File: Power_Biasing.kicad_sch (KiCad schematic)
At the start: 1 part

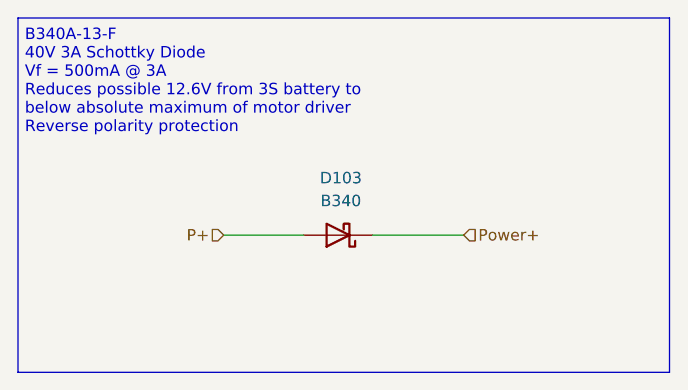
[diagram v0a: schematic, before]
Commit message: added fuse and made power nets thicker
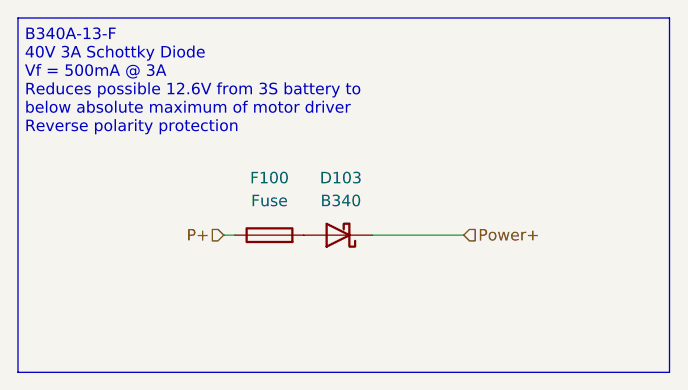
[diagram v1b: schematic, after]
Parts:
- added F100: Fuse, Fuse:Fuse_1206_3216Metric, symbol Device:Fuse
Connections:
- net P+: now also F100.1; no longer D103.2 (A)
- new net: D103.2 (A), F100.2
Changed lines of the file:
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@@
 	(wire
 		(pts
-			(xy 139.7 96.52) (xy 148.59 96.52)
+			(xy 139.7 96.52) (xy 140.97 96.52)
 		)
 		(stroke
@@
 					(unit 1)
 				)
+			)
+		)
+	)
+	(symbol
+		(lib_id "Device:Fuse")
+		(at 144.78 96.52 90)
+		(unit 1)
+		(exclude_from_sim no)
+		(in_bom yes)
+		(on_board yes)
+		(dnp no)
+		(fields_autoplaced yes)
+		(property "Reference" "F100"
+			(at 144.78 90.17 90)
+			(effects
+				(font
+					(size 1.27 1.27)
+				)
+			)
+		)
+		(property "Value" "Fuse"
+			(at 144.78 92.71 90)
+			(effects
+				(font
+					(size 1.27 1.27)
+				)
+			)
+		)
+		(property "Footprint" "Fuse:Fuse_1206_3216Metric"
+			(at 144.78 98.298 90)
+			(effects
+				(font
+					(size 1.27 1.27)
+				)
+				(hide yes)
+			)
+		)
+		(property "Datasheet" "~"
+			(at 144.78 96.52 0)
+			(effects
+				(font
+					(size 1.27 1.27)
+				)
+				(hide yes)
+			)
+		)
+		(property "Description" "Fuse"
+			(at 144.78 96.52 0)
+			(effects
+				(font
+					(size 1.27 1.27)
+				)
+				(hide yes)
+			)
+		)
+		(property "DIGIKEY LINK" "https://www.digikey.com/en/products/detail/bel-fuse-inc/0685H9100-01/5466705"
+			(at 144.78 96.52 90)
+			(effects
+				(font
+					(size 1.27 1.27)
+				)
+				(hide yes)
+			)
+		)
+		(pin "1"
+		)
+		(pin "2"
+		)
+		(instances
+			(project ""
+				(path "/11737956-c422-45b5-a9a0-ee63a853502c/91dc7722-8943-479b-9672-11a66c9c8ce6"
+					(reference "F100")
+					(unit 1)
+				)
